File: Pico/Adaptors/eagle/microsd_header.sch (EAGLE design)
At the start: 3 parts

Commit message: minor board tweaks
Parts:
- R1: value (none) -> 100k
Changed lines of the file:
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@@
 <parts>
 <part name="J1" library="OPL Eagle Library" deviceset="MICRO-SDCARD-CONNECTOR" device="-3300060P1"/>
-<part name="R1" library="rcl" deviceset="R-EU_" device="R1206"/>
+<part name="R1" library="rcl" deviceset="R-EU_" device="R1206" value="100k"/>
 <part name="U$1" library="espruino_pico" deviceset="ESPRUINO_PICO_0.1" device=""/>
 </parts>

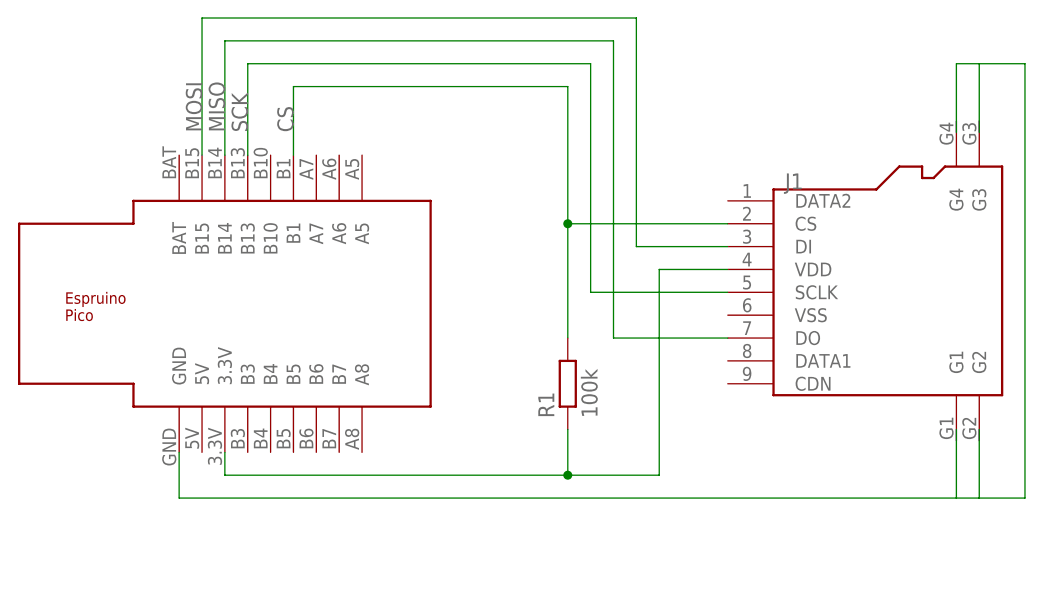
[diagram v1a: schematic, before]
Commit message: fixes for SD card adaptor
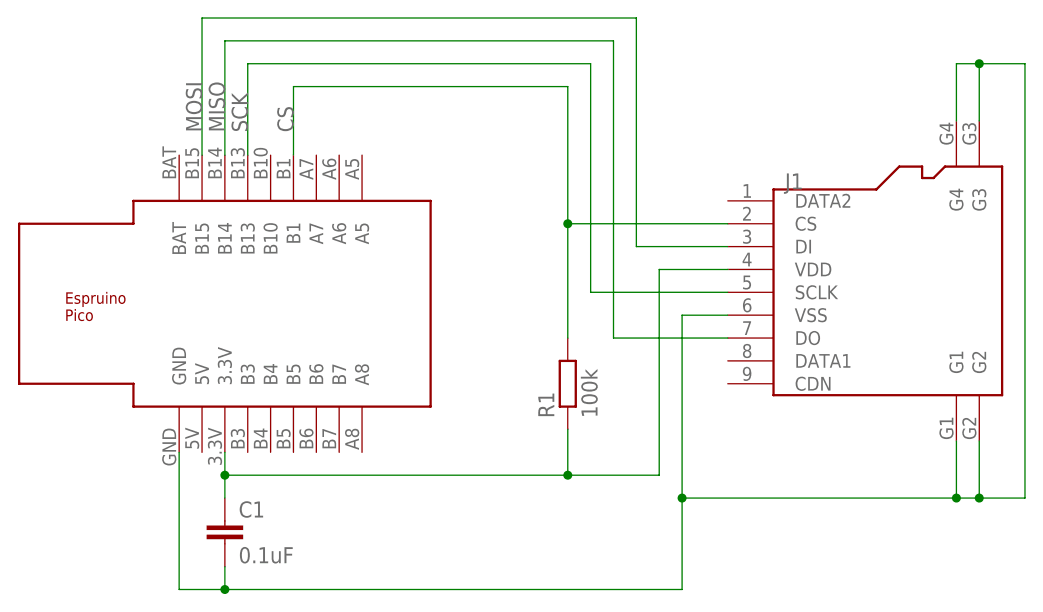
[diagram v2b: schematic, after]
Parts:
- added C1: 0.1uF, rcl:C-EUC1206
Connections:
- removed net N$2: U$1.GND
- new net GND: C1.2, J1.G1, J1.G2, J1.G3, J1.G4, J1.VSS, U$1.GND
- net 3.3V: now also C1.1
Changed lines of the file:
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@@
 <layers>
 <layer number="1" name="Top" color="4" fill="1" visible="no" active="no"/>
+<layer number="2" name="Route2" color="1" fill="3" visible="no" active="no"/>
+<layer number="15" name="Route15" color="4" fill="6" visible="no" active="no"/>
 <layer number="16" name="Bottom" color="1" fill="1" visible="no" active="no"/>
 <layer number="17" name="Pads" color="2" fill="1" visible="no" active="no"/>
@@
 <part name="R1" library="rcl" deviceset="R-EU_" device="R1206" value="100k"/>
 <part name="U$1" library="espruino_pico" deviceset="ESPRUINO_PICO_0.1" device=""/>
+<part name="C1" library="rcl" deviceset="C-EU" device="C1206" value="0.1uF"/>
 </parts>
 <sheets>
@@
 <instance part="R1" gate="G$1" x="78.74" y="7.62" rot="R90"/>
 <instance part="U$1" gate="G$1" x="48.26" y="15.24"/>
+<instance part="C1" gate="G$1" x="40.64" y="-7.62"/>
 </instances>
 <busses>
 </busses>
 <nets>
-<net name="N$2" class="0">
+<net name="GND" class="0">
 <segment>
-<wire x1="121.92" y1="35.56" x2="121.92" y2="43.18" width="0.1524" layer="91"/>
+<wire x1="121.92" y1="36.83" x2="121.92" y2="43.18" width="0.1524" layer="91"/>
 <wire x1="121.92" y1="43.18" x2="124.46" y2="43.18" width="0.1524" layer="91"/>
-<wire x1="124.46" y1="43.18" x2="124.46" y2="35.56" width="0.1524" layer="91"/>
+<wire x1="124.46" y1="43.18" x2="124.46" y2="36.83" width="0.1524" layer="91"/>
 <wire x1="124.46" y1="43.18" x2="129.54" y2="43.18" width="0.1524" layer="91"/>
 <wire x1="129.54" y1="43.18" x2="129.54" y2="-5.08" width="0.1524" layer="91"/>
-<wire x1="121.92" y1="2.54" x2="121.92" y2="-5.08" width="0.1524" layer="91"/>
+<wire x1="121.92" y1="1.27" x2="121.92" y2="-5.08" width="0.1524" layer="91"/>
 <wire x1="121.92" y1="-5.08" x2="124.46" y2="-5.08" width="0.1524" layer="91"/>
-<wire x1="124.46" y1="-5.08" x2="124.46" y2="2.54" width="0.1524" layer="91"/>
+<wire x1="124.46" y1="-5.08" x2="124.46" y2="1.27" width="0.1524" layer="91"/>
 <wire x1="129.54" y1="-5.08" x2="124.46" y2="-5.08" width="0.1524" layer="91"/>
-<wire x1="121.92" y1="-5.08" x2="35.56" y2="-5.08" width="0.1524" layer="91"/>
-<wire x1="35.56" y1="-5.08" x2="35.56" y2="0" width="0.1524" layer="91"/>
+<wire x1="121.92" y1="-5.08" x2="91.44" y2="-5.08" width="0.1524" layer="91"/>
+<wire x1="91.44" y1="-15.24" x2="40.64" y2="-15.24" width="0.1524" layer="91"/>
+<wire x1="40.64" y1="-15.24" x2="35.56" y2="-15.24" width="0.1524" layer="91"/>
+<wire x1="35.56" y1="-15.24" x2="35.56" y2="0" width="0.1524" layer="91"/>
 <pinref part="U$1" gate="G$1" pin="GND"/>
+<pinref part="J1" gate="G$1" pin="VSS"/>
+<wire x1="96.52" y1="15.24" x2="91.44" y2="15.24" width="0.1524" layer="91"/>
+<wire x1="91.44" y1="15.24" x2="91.44" y2="-5.08" width="0.1524" layer="91"/>
+<junction x="121.92" y="-5.08"/>
+<junction x="124.46" y="-5.08"/>
+<junction x="124.46" y="43.18"/>
+<pinref part="J1" gate="G$1" pin="G4"/>
+<pinref part="J1" gate="G$1" pin="G3"/>
+<pinref part="J1" gate="G$1" pin="G1"/>
+<pinref part="J1" gate="G$1" pin="G2"/>
+<pinref part="C1" gate="G$1" pin="2"/>
+<wire x1="91.44" y1="-5.08" x2="91.44" y2="-15.24" width="0.1524" layer="91"/>
+<wire x1="40.64" y1="-12.7" x2="40.64" y2="-15.24" width="0.1524" layer="91"/>
+<junction x="91.44" y="-5.08"/>
+<junction x="40.64" y="-15.24"/>
 </segment>
 </net>
@@
 <pinref part="J1" gate="G$1" pin="VDD"/>
 <wire x1="88.9" y1="20.32" x2="96.52" y2="20.32" width="0.1524" layer="91"/>
+<pinref part="U$1" gate="G$1" pin="3.3V"/>
+<pinref part="C1" gate="G$1" pin="1"/>
+<wire x1="40.64" y1="-2.54" x2="40.64" y2="-5.08" width="0.1524" layer="91"/>
+<junction x="40.64" y="-2.54"/>
 <pinref part="R1" gate="G$1" pin="1"/>
 <wire x1="78.74" y1="2.54" x2="78.74" y2="-2.54" width="0.1524" layer="91"/>
 <junction x="78.74" y="-2.54"/>
-<pinref part="U$1" gate="G$1" pin="3.3V"/>
 </segment>
 </net>
